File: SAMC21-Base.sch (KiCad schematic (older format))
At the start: 56 parts, among them J1 Conn_01x04, J2 Conn_01x10, J3 Conn_01x10, J5 Conn_ARM_JTAG_SWD_10, U1 ATSAMC21E18A-AUT, U2 TJA1043T, U3 TPS560430Y, U4 MCP1703A, Y1 ABM3-8.000MHZ-D2Y-T

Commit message: rework power stage, again.
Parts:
- added R13: 100K, Resistor_SMD:R_0603_1608Metric, symbol Device:R_Small
- C1, C20: value 10uF/50V -> 4.7uF/50V
- D1: value MBR0560 -> 60V 1A; MPN (none) -> RB160MM-60TFTR
- D3: value SMAJ40A -> 36V; MPN (none) -> SMAJ36CA
- F1: value 1812L020/60 -> 60V 200mA; MPN (none) -> 1812L020/60
- L1: value NR5040T100M -> SRN4018-100M; footprint Inductor_SMD:L_Taiyo-Yuden_NR-50xx -> Inductor_SMD:L_Bourns-SRN4018
- L3: value MLP2012V4R7MT0S1 -> 4.7uH; MPN (none) -> MLP2012V4R7MT0S1
- R1: value 100K -> 15K
- RT1, RT2: footprint Resistor_SMD:R_0603_1608Metric -> Resistor_SMD:R_0805_2012Metric
- U3: value TPS560430Y -> LMR50410-Q1; symbol Hausbus-Regulator_Switching:TPS560430 -> Hausbus-Regulator_Switching:LMR50410-Q1
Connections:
- net +36V: now also D1.1 (K), L3.1; no longer C2.1, C20.1, L3.2, U3.5 (VIN)
- net INH: now also R13.1; no longer R1.1, U3.4 (EN)
- new net: C2.1, C20.1, L3.2, U3.5 (VIN)
- new net EN: R1.1, R13.2, U3.4 (EN)
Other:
- note added: "EN at VIN>9V"
- note added: "uC operating voltage 3V3 or 5V"
- note removed: "choose operating voltage"
- moved on the sheet: C1, C10, C11, C12, C13, C18, C19, C2, C20, C3, C5, C6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

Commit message: polish schematics
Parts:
- added C18: 2.2nF, Capacitor_SMD:C_0603_1608Metric, symbol Device:C_Small
- added J4: Conn_01x04, Connector_PinHeader_2.54mm:PinHeader_1x04_P2.54mm_Vertical, symbol Connector_Generic:Conn_01x04
- added TP1, TP2, TP3, TP4, TP5: TestPoint, symbol Connector:TestPoint
- C3: value 10uF -> 10uF/10V
- C4: renamed from C5; value 10uF -> 10uF/10V
- C5: renamed from C6; value 10uF -> 10uF/10V
- C6: renamed from C7; value 10uF -> 10uF/10V
- C7: renamed from C8; value 10uF -> 10uF/10V
- C9: renamed from C16; value 100nF/50V -> 100nF/100V
- H1, H2, H3, H4: footprint MountingHole:MountingHole_2mm -> MountingHole:MountingHole_3.2mm_M3
- J2, J3: symbol Connector_Generic:Conn_01x10 -> Connector_Generic:Conn_01x12
- L2: renamed from L1; value SRN4018-100M -> 10uH; MPN (none) -> SRN4018-100M
- L3: renamed from L2; value MPZ1608S221A -> 220R@100MHz; MPN (none) -> MPZ1608S221ATA00
- R10: value 10K -> 6K8
- RV1, RV2: value CT0805K25G -> 25V; MPN (none) -> CT0805K25G
- Y1: value ABM3-8.000MHZ-D2Y-T -> 8MHz; MPN (none) -> ABM3-8.000MHZ-D2Y-T
- renumbered C9 to C116, C18 to C19, C20 to C2, C19 to C20, C2 to C8, D3 to D1, D1 to D2, L3 to L1, D2 to LED1
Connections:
- net +36V: no longer R9.1
- net +3V3: now also J2.5 (Pin_5); no longer J2.3 (Pin_3)
- net +5V: now also J2.3 (Pin_3); no longer J2.2 (Pin_2)
- net CAN_H: now also J4.2 (Pin_2)
- net CAN_L: now also RV2.2, J4.3 (Pin_3); no longer RV2.1
- net EN: now also C18.1
- net GND: now also J2.12 (Pin_12), J2.2 (Pin_2), J2.4 (Pin_4), J2.6 (Pin_6), J3.11 (Pin_11), J3.6 (Pin_6), RV2.1, C18.2, J4.4 (Pin_4), TP5.1; no longer J2.7 (Pin_7), J2.9 (Pin_9), RV2.2
- net INH: now also J2.9 (Pin_9); no longer J2.5 (Pin_5)
- net PA02: now also J3.12 (Pin_12); no longer J3.10 (Pin_10)
- net PA04: now also J3.10 (Pin_10); no longer J3.9 (Pin_9)
- net PA05: now also J3.9 (Pin_9); no longer J3.8 (Pin_8)
- net PA06: now also J3.8 (Pin_8); no longer J3.7 (Pin_7)
- net PA07: now also J3.7 (Pin_7); no longer J3.6 (Pin_6)
- net RESET: now also TP1.1
- net SWDCLK: now also TP2.1
- net SWDIO: now also TP3.1
- net VBUS: now also R9.1, J4.1 (Pin_1)
- net VDD: now also J2.7 (Pin_7), TP4.1; no longer J2.4 (Pin_4)
- net WAKE: now also J2.11 (Pin_11); no longer J2.6 (Pin_6)
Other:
- note added: "after <1ms"
- moved on the sheet: C1, C10, C11, C116, C12, C13, C14, C15, C17, C19, C2, C20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

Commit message: redo layout. from scratch.
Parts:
- removed J4: Conn_01x04, Connector_PinHeader_2.54mm:PinHeader_1x04_P2.54mm_Vertical, symbol Connector_Generic:Conn_01x04
- H1, H2, H3, H4: footprint MountingHole:MountingHole_3.2mm_M3 -> MountingHole:MountingHole_2.2mm_M2
- J2, J3: footprint Connector_PinHeader_2.54mm:PinHeader_1x10_P2.54mm_Vertical -> Connector_PinHeader_2.54mm:PinHeader_1x12_P2.54mm_Vertical
- TP1, TP2, TP3, TP4, TP5: footprint (none) -> TestPoint:TestPoint_Pad_D1.5mm
- renumbered C116 to C16
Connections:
- net CAN_STB: now also U1.23 (PA24); no longer U1.24 (PA25)
- net CB: now reaches C10.2, U3.1 (CB)
- net FB: now reaches R7.2, R8.1, U3.3 (FB)
- net DCDC_IN: now reaches C2.1, C8.1, L1.2, U3.5 (VIN)
- net SW: now reaches C10.1, L2.1, U3.6 (SW)
- net at U1.1 (PA00): no longer LED1.1 (K)
- new net LED: LED1.1 (K), U1.24 (PA25)
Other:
- moved on the sheet: J2, J3, LED1, R11

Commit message: cleanup after review-3
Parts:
- C19, C20: value 18pF -> 33pF
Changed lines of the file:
@@
 U 1 1 60907F03
 P 10600 4650
-F 0 "C20" V 10700 4750 50  0000 R CNN
-F 1 "18pF" V 10500 4650 50  0000 C CNN
+F 0 "C20" V 10700 4650 50  0000 C CNN
+F 1 "33pF" V 10500 4650 50  0000 C CNN
 F 2 "Capacitor_SMD:C_0603_1608Metric" H 10600 4650 50  0001 C CNN
 F 3 "~" H 10600 4650 50  0001 C CNN
@@
 U 1 1 60909D78
 P 10100 4650
-F 0 "C19" V 10200 4600 50  0000 L CNN
-F 1 "18pF" V 10000 4650 50  0000 C CNN
+F 0 "C19" V 10200 4650 50  0000 C CNN
+F 1 "33pF" V 10000 4650 50  0000 C CNN
 F 2 "Capacitor_SMD:C_0603_1608Metric" H 10100 4650 50  0001 C CNN
 F 3 "~" H 10100 4650 50  0001 C CNN

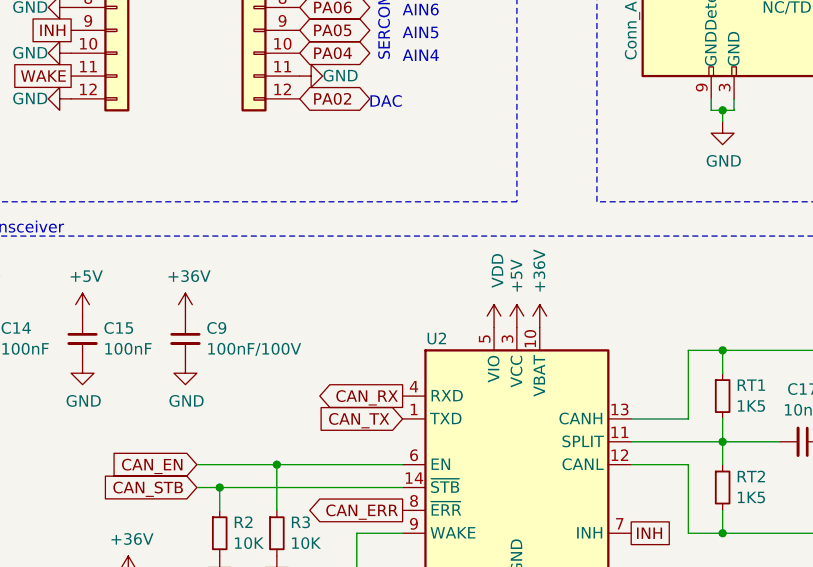
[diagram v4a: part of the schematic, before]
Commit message: use DCDC_IN for TJA1043 Vbat
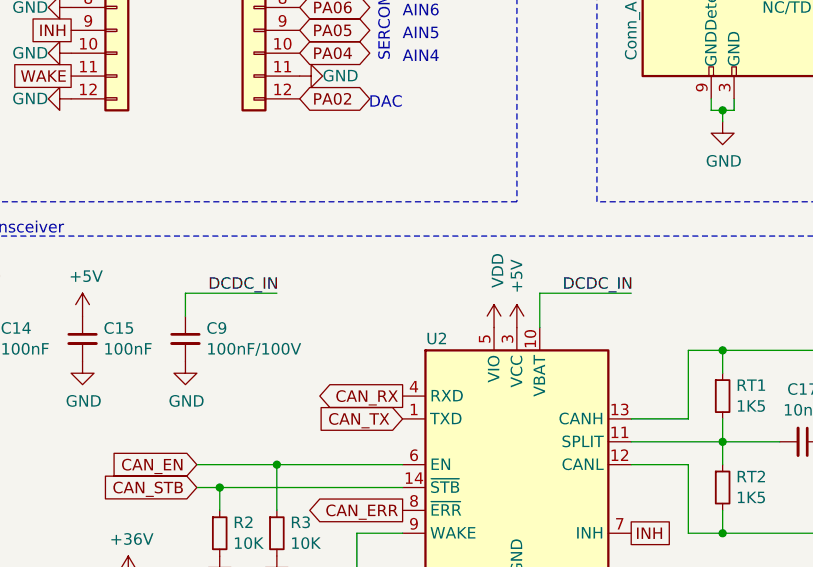
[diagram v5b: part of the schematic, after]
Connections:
- net +36V: no longer C9.1, U2.10 (VBAT)
- net DCDC_IN: now also C9.1, U2.10 (VBAT)
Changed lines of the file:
@@
-$EndComp
-$Comp
-L power:+36V #PWR011
-U 1 1 6081FE41
-P 2000 5650
-F 0 "#PWR011" H 2000 5500 50  0001 C CNN
-F 1 "+36V" H 2015 5823 50  0000 C CNN
-F 2 "" H 2000 5650 50  0001 C CNN
-F 3 "" H 2000 5650 50  0001 C CNN
-	1    2000 5650
-	1    0    0    -1
 $EndComp
 $Comp
@@
 F 3 "" H 3450 5700 50  0001 C CNN
 	1    3450 5700
-	1    0    0    -1
-$EndComp
-$Comp
-L power:+36V #PWR018
-U 1 1 60839AB7
-P 3550 5700
-F 0 "#PWR018" H 3550 5550 50  0001 C CNN
-F 1 "+36V" V 3550 5850 50  0000 L CNN
-F 2 "" H 3550 5700 50  0001 C CNN
-F 3 "" H 3550 5700 50  0001 C CNN
-	1    3550 5700
 	1    0    0    -1
 $EndComp
@@
 $EndComp
 $Comp
-L power:PWR_FLAG #FLG01
-U 1 1 606C55C2
-P 2700 1350
-F 0 "#FLG01" H 2700 1425 50  0001 C CNN
-F 1 "PWR_FLAG" H 2700 1523 50  0001 C CNN
-F 2 "" H 2700 1350 50  0001 C CNN
-F 3 "~" H 2700 1350 50  0001 C CNN
-	1    2700 1350
-	-1   0    0    1
-$EndComp
-$Comp
-L power:+36V #PWR05
-U 1 1 606BF4B9
-P 2700 1300
-F 0 "#PWR05" H 2700 1150 50  0001 C CNN
-F 1 "+36V" H 2700 1500 50  0000 C CNN
-F 2 "" H 2700 1300 50  0001 C CNN
-F 3 "" H 2700 1300 50  0001 C CNN
-	1    2700 1300
-	1    0    0    -1
-$EndComp
-$Comp
 L Mechanical:MountingHole H4
 U 1 1 6077C62D
@@
 Wire Notes Line
 	10850 700  10850 2850
-Connection ~ 2700 1350
-Wire Wire Line
-	2700 1350 2500 1350
-Wire Wire Line
-	2700 1300 2700 1350
 Wire Wire Line
 	6350 1350 6750 1350
@@
 EN at VIN>9V
 Connection ~ 2950 1350
-Wire Wire Line
-	2950 1350 2700 1350
 Wire Wire Line
 	2950 1350 3150 1350
@@
 	1    0    0    -1
 $EndComp
-Text Label 4050 1350 0    50   ~ 0
-DCDC_IN
 Text Label 5650 1350 0    50   ~ 0
 CB
@@
 LED
 NoConn ~ 7550 4300
+Wire Wire Line
+	2950 1350 2700 1350
+Wire Wire Line
+	2700 1350 2500 1350
+Connection ~ 2700 1350
+$Comp
+L power:PWR_FLAG #FLG01
+U 1 1 606C55C2
+P 2700 1350
+F 0 "#FLG01" H 2700 1425 50  0001 C CNN
+F 1 "PWR_FLAG" H 2700 1523 50  0001 C CNN
+F 2 "" H 2700 1350 50  0001 C CNN
+F 3 "~" H 2700 1350 50  0001 C CNN
+	1    2700 1350
+	-1   0    0    1
+$EndComp
+Text Label 4050 1350 0    50   ~ 0
+DCDC_IN
+Wire Wire Line
+	2700 1300 2700 1350
+$Comp
+L power:+36V #PWR05
+U 1 1 606BF4B9
+P 2700 1300
+F 0 "#PWR05" H 2700 1150 50  0001 C CNN
+F 1 "+36V" H 2700 1500 50  0000 C CNN
+F 2 "" H 2700 1300 50  0001 C CNN
+F 3 "" H 2700 1300 50  0001 C CNN
+	1    2700 1300
+	1    0    0    -1
+$EndComp
+Text Label 2100 5550 0    50   ~ 0
+DCDC_IN
+Wire Wire Line
+	3550 5700 3550 5550
+Wire Wire Line
+	2000 5550 2400 5550
+Wire Wire Line
+	2000 5550 2000 5650
+Text Label 3650 5550 0    50   ~ 0
+DCDC_IN
+Wire Wire Line
+	3550 5550 3950 5550
 $EndSCHEMATC
